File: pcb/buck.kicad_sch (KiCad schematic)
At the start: 14 parts, among them U1 TPSM863257

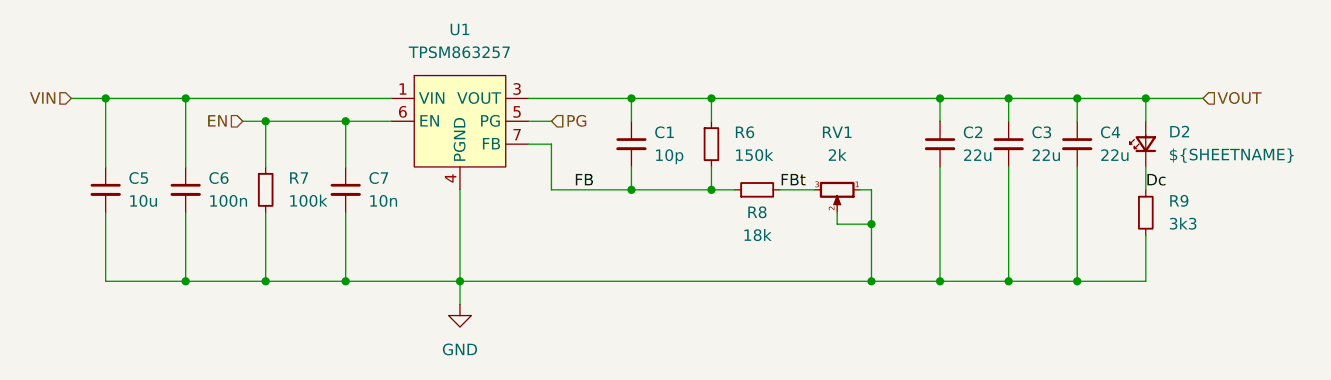
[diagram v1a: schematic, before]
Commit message: feat: add more functionality
- INA power monitor on each output
- I/O expander to reset usb ports if needed
- Bratwurst Logo
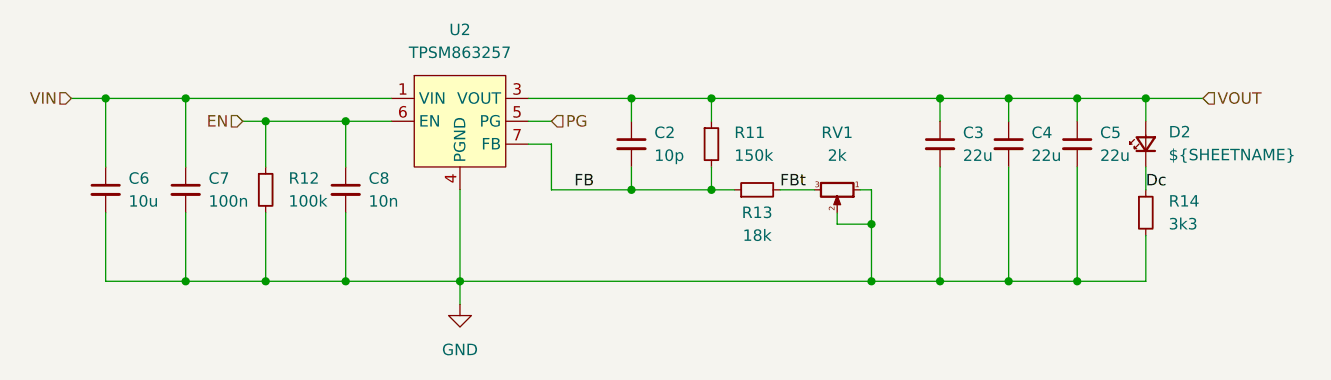
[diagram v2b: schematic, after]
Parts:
- renumbered C1 to C2, C2 to C3, C3 to C4, C4 to C5, C5 to C6, C6 to C7, C7 to C8, R6 to R11, R7 to R12, R8 to R13, R9 to R14, U1 to U2

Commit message: fix: change pots to 2.2kΩ
fix: part numbers
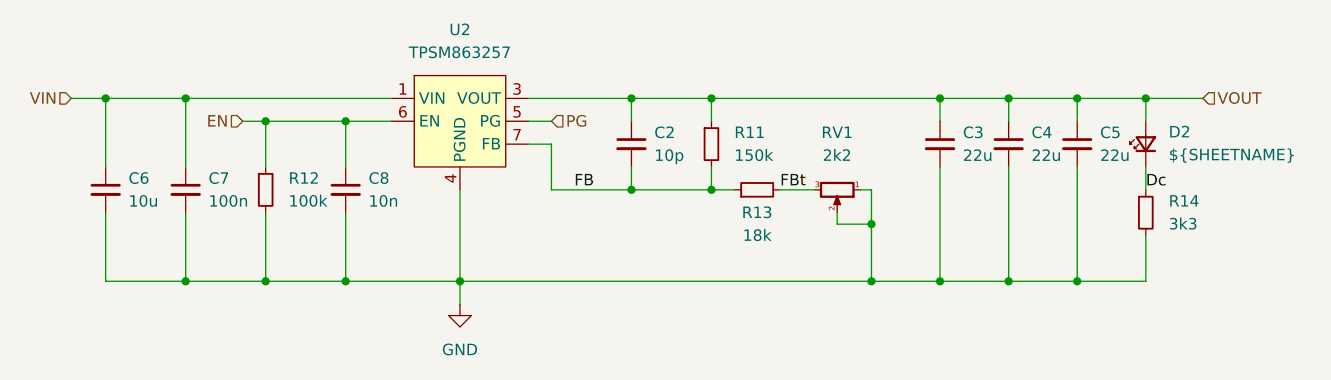
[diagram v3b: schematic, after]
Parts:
- R13: LCSC C25765 -> C25762
- RV1: value 2k -> 2k2; LCSC C128549 -> C145162
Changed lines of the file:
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@@
 			)
 		)
-		(property "LCSC" "C25765"
+		(property "LCSC" "C25762"
 			(at 170.18 92.71 0)
 			(effects
@@
 			)
 		)
-		(property "Value" "2k"
+		(property "Value" "2k2"
 			(at 179.07 88.9 90)
 			(effects
@@
 			)
 		)
-		(property "LCSC" "C128549"
+		(property "LCSC" "C145162"
 			(at 179.07 92.71 0)
 			(effects
